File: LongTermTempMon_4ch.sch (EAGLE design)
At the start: 26 parts, among them IC2 LTC2418

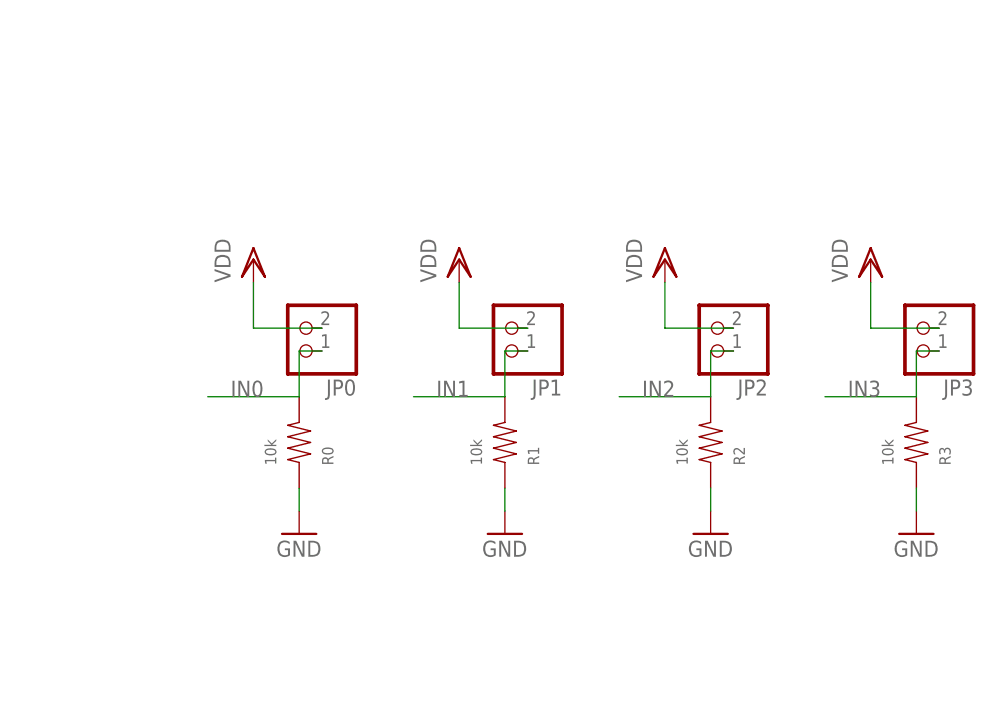
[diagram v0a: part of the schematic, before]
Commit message: Modified circuit to have reference resistor tied to +5V instead of Gnd
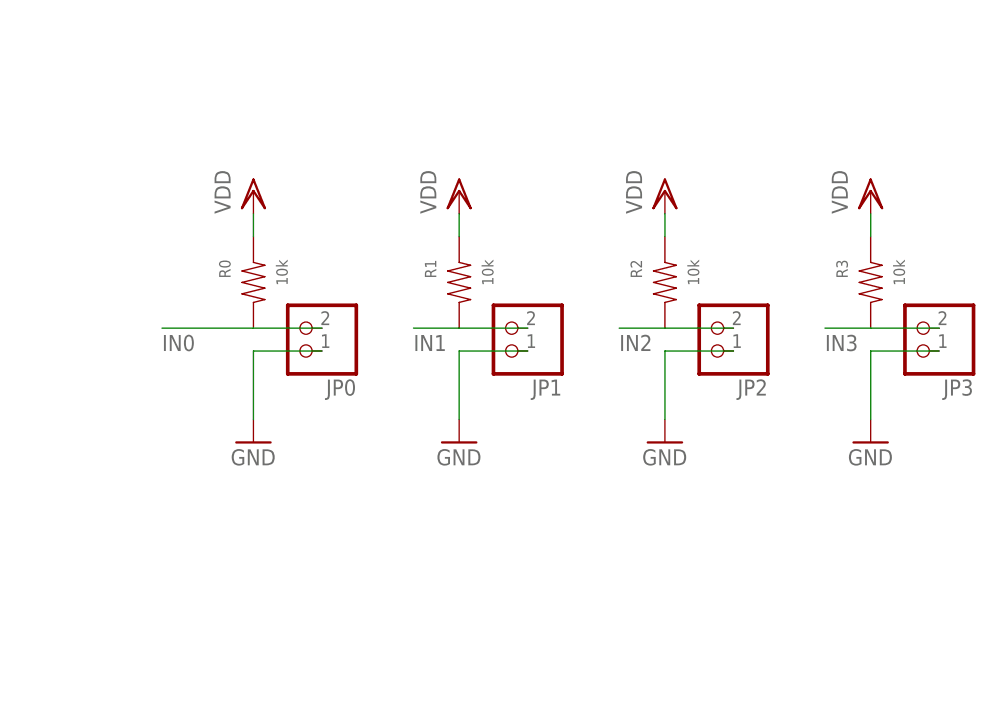
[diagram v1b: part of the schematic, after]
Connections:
- net GND: now also JP0.1, JP1.1, JP2.1, JP3.1; no longer R0.P$1, R1.P$1, R2.P$1, R3.P$1
- net IN0: now also JP0.2; no longer JP0.1
- net IN1: now also JP1.2; no longer JP1.1
- net IN2: now also JP2.2; no longer JP2.1
- net IN3: now also JP3.2; no longer JP3.1
- net VDD: now also R0.P$1, R1.P$1, R2.P$1, R3.P$1; no longer JP0.2, JP1.2, JP2.2, JP3.2
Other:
- moved on the sheet: R0, R1, R2, R3
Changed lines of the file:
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@@
 <instances>
 <instance part="U$1" gate="G$1" x="25.4" y="0"/>
-<instance part="R0" gate="G$1" x="96.52" y="-38.1" rot="MR90"/>
+<instance part="R0" gate="G$1" x="91.44" y="-20.32" rot="MR270"/>
 <instance part="VDD13" gate="G$1" x="-14.986" y="-99.06"/>
 <instance part="C10" gate="G$1" x="-5.08" y="-111.76" rot="R90"/>
@@
 <instance part="VDD11" gate="G$1" x="88.9" y="63.5"/>
 <instance part="L2" gate="G$1" x="78.74" y="50.8"/>
-<instance part="GND" gate="1" x="96.52" y="-48.26"/>
+<instance part="GND" gate="1" x="91.44" y="-38.1"/>
 <instance part="CP1" gate="G$1" x="-22.86" y="83.82"/>
 <instance part="CP3" gate="G$1" x="45.72" y="83.82"/>
@@
 <instance part="L1" gate="G$1" x="-33.02" y="-76.2"/>
 <instance part="VDD1" gate="G$1" x="-40.64" y="-71.12"/>
-<instance part="VDD2" gate="G$1" x="91.44" y="-17.78"/>
-<instance part="R1" gate="G$1" x="119.38" y="-38.1" rot="MR90"/>
+<instance part="VDD2" gate="G$1" x="91.44" y="-10.16"/>
+<instance part="R1" gate="G$1" x="114.3" y="-20.32" rot="MR270"/>
 <instance part="JP1" gate="G$1" x="119.38" y="-25.4" rot="R180"/>
-<instance part="GND1" gate="1" x="119.38" y="-48.26"/>
-<instance part="VDD3" gate="G$1" x="114.3" y="-17.78"/>
-<instance part="R2" gate="G$1" x="142.24" y="-38.1" rot="MR90"/>
+<instance part="GND1" gate="1" x="114.3" y="-38.1"/>
+<instance part="VDD3" gate="G$1" x="114.3" y="-10.16"/>
+<instance part="R2" gate="G$1" x="137.16" y="-20.32" rot="MR270"/>
 <instance part="JP2" gate="G$1" x="142.24" y="-25.4" rot="R180"/>
-<instance part="GND3" gate="1" x="142.24" y="-48.26"/>
-<instance part="VDD4" gate="G$1" x="137.16" y="-17.78"/>
-<instance part="R3" gate="G$1" x="165.1" y="-38.1" rot="MR90"/>
+<instance part="GND3" gate="1" x="137.16" y="-38.1"/>
+<instance part="VDD4" gate="G$1" x="137.16" y="-10.16"/>
+<instance part="R3" gate="G$1" x="160.02" y="-20.32" rot="MR270"/>
 <instance part="JP3" gate="G$1" x="165.1" y="-25.4" rot="R180"/>
-<instance part="GND7" gate="1" x="165.1" y="-48.26"/>
-<instance part="VDD5" gate="G$1" x="160.02" y="-17.78"/>
+<instance part="GND7" gate="1" x="160.02" y="-38.1"/>
+<instance part="VDD5" gate="G$1" x="160.02" y="-10.16"/>
 <instance part="C1" gate="G$1" x="71.12" y="-91.44" rot="R90"/>
 <instance part="C2" gate="G$1" x="78.74" y="-86.36" rot="R90"/>
@@
 </segment>
 <segment>
-<wire x1="99.06" y1="-25.4" x2="91.44" y2="-25.4" width="0.1524" layer="91"/>
-<pinref part="JP0" gate="G$1" pin="2"/>
-<wire x1="91.44" y1="-25.4" x2="91.44" y2="-20.32" width="0.1524" layer="91"/>
+<wire x1="91.44" y1="-15.24" x2="91.44" y2="-12.7" width="0.1524" layer="91"/>
 <pinref part="VDD2" gate="G$1" pin="VDD"/>
-</segment>
-<segment>
-<wire x1="121.92" y1="-25.4" x2="114.3" y2="-25.4" width="0.1524" layer="91"/>
-<pinref part="JP1" gate="G$1" pin="2"/>
-<wire x1="114.3" y1="-25.4" x2="114.3" y2="-20.32" width="0.1524" layer="91"/>
+<pinref part="R0" gate="G$1" pin="P$1"/>
+</segment>
+<segment>
+<wire x1="114.3" y1="-15.24" x2="114.3" y2="-12.7" width="0.1524" layer="91"/>
 <pinref part="VDD3" gate="G$1" pin="VDD"/>
-</segment>
-<segment>
-<wire x1="144.78" y1="-25.4" x2="137.16" y2="-25.4" width="0.1524" layer="91"/>
-<pinref part="JP2" gate="G$1" pin="2"/>
-<wire x1="137.16" y1="-25.4" x2="137.16" y2="-20.32" width="0.1524" layer="91"/>
+<pinref part="R1" gate="G$1" pin="P$1"/>
+</segment>
+<segment>
+<wire x1="137.16" y1="-15.24" x2="137.16" y2="-12.7" width="0.1524" layer="91"/>
 <pinref part="VDD4" gate="G$1" pin="VDD"/>
-</segment>
-<segment>
-<wire x1="167.64" y1="-25.4" x2="160.02" y2="-25.4" width="0.1524" layer="91"/>
-<pinref part="JP3" gate="G$1" pin="2"/>
-<wire x1="160.02" y1="-25.4" x2="160.02" y2="-20.32" width="0.1524" layer="91"/>
+<pinref part="R2" gate="G$1" pin="P$1"/>
+</segment>
+<segment>
+<wire x1="160.02" y1="-15.24" x2="160.02" y2="-12.7" width="0.1524" layer="91"/>
 <pinref part="VDD5" gate="G$1" pin="VDD"/>
+<pinref part="R3" gate="G$1" pin="P$1"/>
 </segment>
 </net>
@@
 </net>
 <net name="GND" class="0">
-<segment>
-<pinref part="GND" gate="1" pin="GND"/>
-<pinref part="R0" gate="G$1" pin="P$1"/>
-<wire x1="96.52" y1="-43.18" x2="96.52" y2="-45.72" width="0.1524" layer="91"/>
-</segment>
 <segment>
 <wire x1="58.42" y1="71.12" x2="58.42" y2="73.66" width="0.1524" layer="91"/>
@@
 </segment>
 <segment>
+<pinref part="JP0" gate="G$1" pin="1"/>
+<pinref part="GND" gate="1" pin="GND"/>
+<wire x1="99.06" y1="-27.94" x2="91.44" y2="-27.94" width="0.1524" layer="91"/>
+<wire x1="91.44" y1="-27.94" x2="91.44" y2="-35.56" width="0.1524" layer="91"/>
+</segment>
+<segment>
+<pinref part="JP1" gate="G$1" pin="1"/>
 <pinref part="GND1" gate="1" pin="GND"/>
-<pinref part="R1" gate="G$1" pin="P$1"/>
-<wire x1="119.38" y1="-43.18" x2="119.38" y2="-45.72" width="0.1524" layer="91"/>
-</segment>
-<segment>
+<wire x1="121.92" y1="-27.94" x2="114.3" y2="-27.94" width="0.1524" layer="91"/>
+<wire x1="114.3" y1="-27.94" x2="114.3" y2="-35.56" width="0.1524" layer="91"/>
+</segment>
+<segment>
+<pinref part="JP2" gate="G$1" pin="1"/>
 <pinref part="GND3" gate="1" pin="GND"/>
-<pinref part="R2" gate="G$1" pin="P$1"/>
-<wire x1="142.24" y1="-43.18" x2="142.24" y2="-45.72" width="0.1524" layer="91"/>
-</segment>
-<segment>
+<wire x1="144.78" y1="-27.94" x2="137.16" y2="-27.94" width="0.1524" layer="91"/>
+<wire x1="137.16" y1="-27.94" x2="137.16" y2="-35.56" width="0.1524" layer="91"/>
+</segment>
+<segment>
+<pinref part="JP3" gate="G$1" pin="1"/>
 <pinref part="GND7" gate="1" pin="GND"/>
-<pinref part="R3" gate="G$1" pin="P$1"/>
-<wire x1="165.1" y1="-43.18" x2="165.1" y2="-45.72" width="0.1524" layer="91"/>
+<wire x1="167.64" y1="-27.94" x2="160.02" y2="-27.94" width="0.1524" layer="91"/>
+<wire x1="160.02" y1="-27.94" x2="160.02" y2="-35.56" width="0.1524" layer="91"/>
 </segment>
 </net>
@@
 </segment>
 <segment>
-<pinref part="JP0" gate="G$1" pin="1"/>
-<wire x1="99.06" y1="-27.94" x2="96.52" y2="-27.94" width="0.1524" layer="91"/>
 <pinref part="R0" gate="G$1" pin="P$2"/>
-<wire x1="96.52" y1="-27.94" x2="96.52" y2="-33.02" width="0.1524" layer="91"/>
-<wire x1="96.52" y1="-33.02" x2="86.36" y2="-33.02" width="0.1524" layer="91"/>
-<label x="88.9" y="-33.02" size="1.778" layer="95"/>
+<wire x1="91.44" y1="-25.4" x2="81.28" y2="-25.4" width="0.1524" layer="91"/>
+<label x="81.28" y="-27.94" size="1.778" layer="95"/>
+<pinref part="JP0" gate="G$1" pin="2"/>
+<wire x1="91.44" y1="-25.4" x2="99.06" y2="-25.4" width="0.1524" layer="91"/>
 </segment>
 </net>
 <net name="IN1" class="0">
 <segment>
-<pinref part="JP1" gate="G$1" pin="1"/>
-<wire x1="121.92" y1="-27.94" x2="119.38" y2="-27.94" width="0.1524" layer="91"/>
 <pinref part="R1" gate="G$1" pin="P$2"/>
-<wire x1="119.38" y1="-27.94" x2="119.38" y2="-33.02" width="0.1524" layer="91"/>
-<wire x1="119.38" y1="-33.02" x2="109.22" y2="-33.02" width="0.1524" layer="91"/>
-<label x="111.76" y="-33.02" size="1.778" layer="95"/>
+<wire x1="114.3" y1="-25.4" x2="109.22" y2="-25.4" width="0.1524" layer="91"/>
+<label x="109.22" y="-27.94" size="1.778" layer="95"/>
+<pinref part="JP1" gate="G$1" pin="2"/>
+<wire x1="114.3" y1="-25.4" x2="121.92" y2="-25.4" width="0.1524" layer="91"/>
 </segment>
 <segment>
@@
 <net name="IN2" class="0">
 <segment>
-<pinref part="JP2" gate="G$1" pin="1"/>
-<wire x1="144.78" y1="-27.94" x2="142.24" y2="-27.94" width="0.1524" layer="91"/>
 <pinref part="R2" gate="G$1" pin="P$2"/>
-<wire x1="142.24" y1="-27.94" x2="142.24" y2="-33.02" width="0.1524" layer="91"/>
-<wire x1="142.24" y1="-33.02" x2="132.08" y2="-33.02" width="0.1524" layer="91"/>
-<label x="134.62" y="-33.02" size="1.778" layer="95"/>
+<wire x1="137.16" y1="-25.4" x2="132.08" y2="-25.4" width="0.1524" layer="91"/>
+<label x="132.08" y="-27.94" size="1.778" layer="95"/>
+<pinref part="JP2" gate="G$1" pin="2"/>
+<wire x1="137.16" y1="-25.4" x2="144.78" y2="-25.4" width="0.1524" layer="91"/>
 </segment>
 <segment>
@@
 <net name="IN3" class="0">
 <segment>
-<pinref part="JP3" gate="G$1" pin="1"/>
-<wire x1="167.64" y1="-27.94" x2="165.1" y2="-27.94" width="0.1524" layer="91"/>
 <pinref part="R3" gate="G$1" pin="P$2"/>
-<wire x1="165.1" y1="-27.94" x2="165.1" y2="-33.02" width="0.1524" layer="91"/>
-<wire x1="165.1" y1="-33.02" x2="154.94" y2="-33.02" width="0.1524" layer="91"/>
-<label x="157.48" y="-33.02" size="1.778" layer="95"/>
-</segment>
-<segment>
+<wire x1="160.02" y1="-25.4" x2="154.94" y2="-25.4" width="0.1524" layer="91"/>
+<label x="154.94" y="-27.94" size="1.778" layer="95"/>
+<pinref part="JP3" gate="G$1" pin="2"/>
+<wire x1="160.02" y1="-25.4" x2="167.64" y2="-25.4" width="0.1524" layer="91"/>
+</segment>
+<segment>
